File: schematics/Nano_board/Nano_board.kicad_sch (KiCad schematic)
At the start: 28 parts, among them J1 Screw_Terminal_01x02, J2 Screw_Terminal_01x02, J3 Screw_Terminal_01x02, J4 Left switch, J5 Right switch, J6 UART, J7 Left encoder, J8 Right encoder

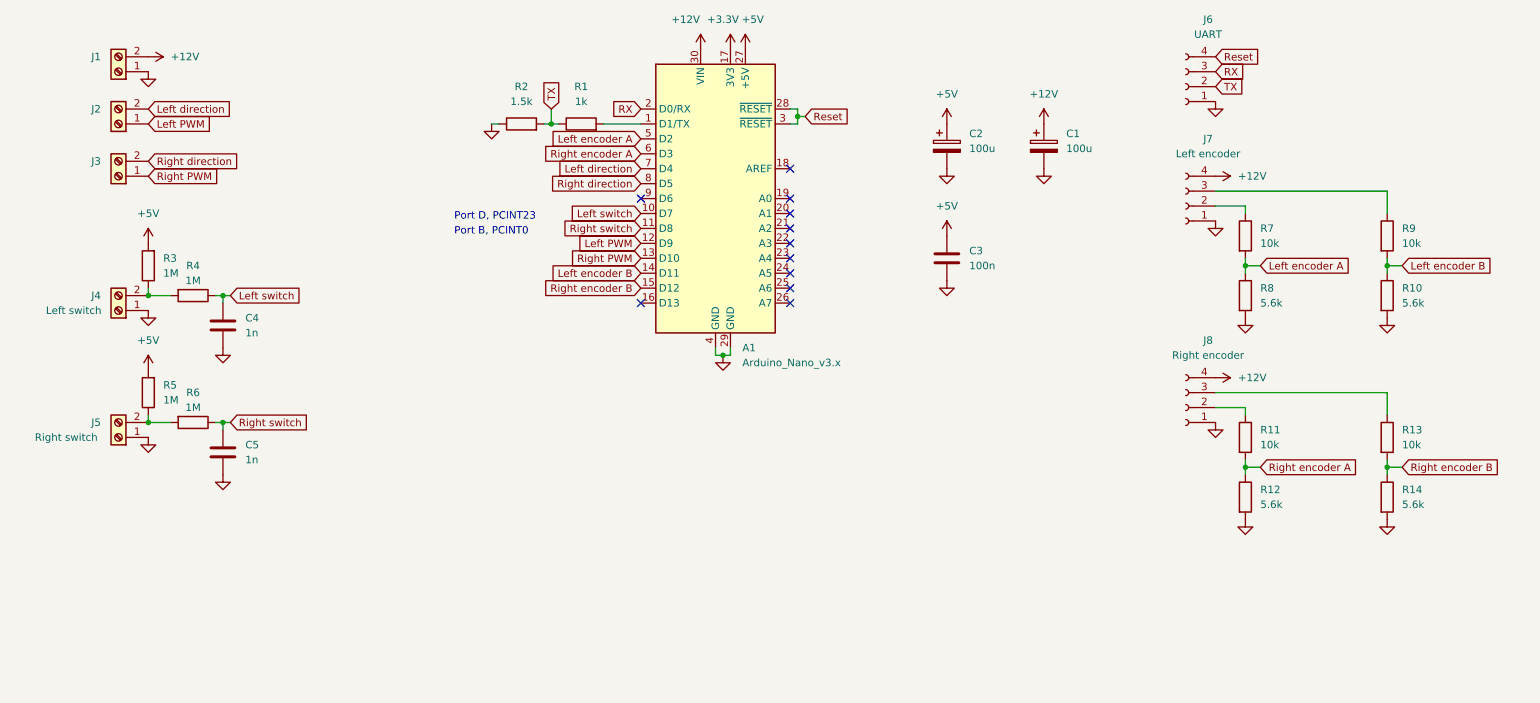
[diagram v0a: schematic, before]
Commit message: feat: updated Nano board schematics.
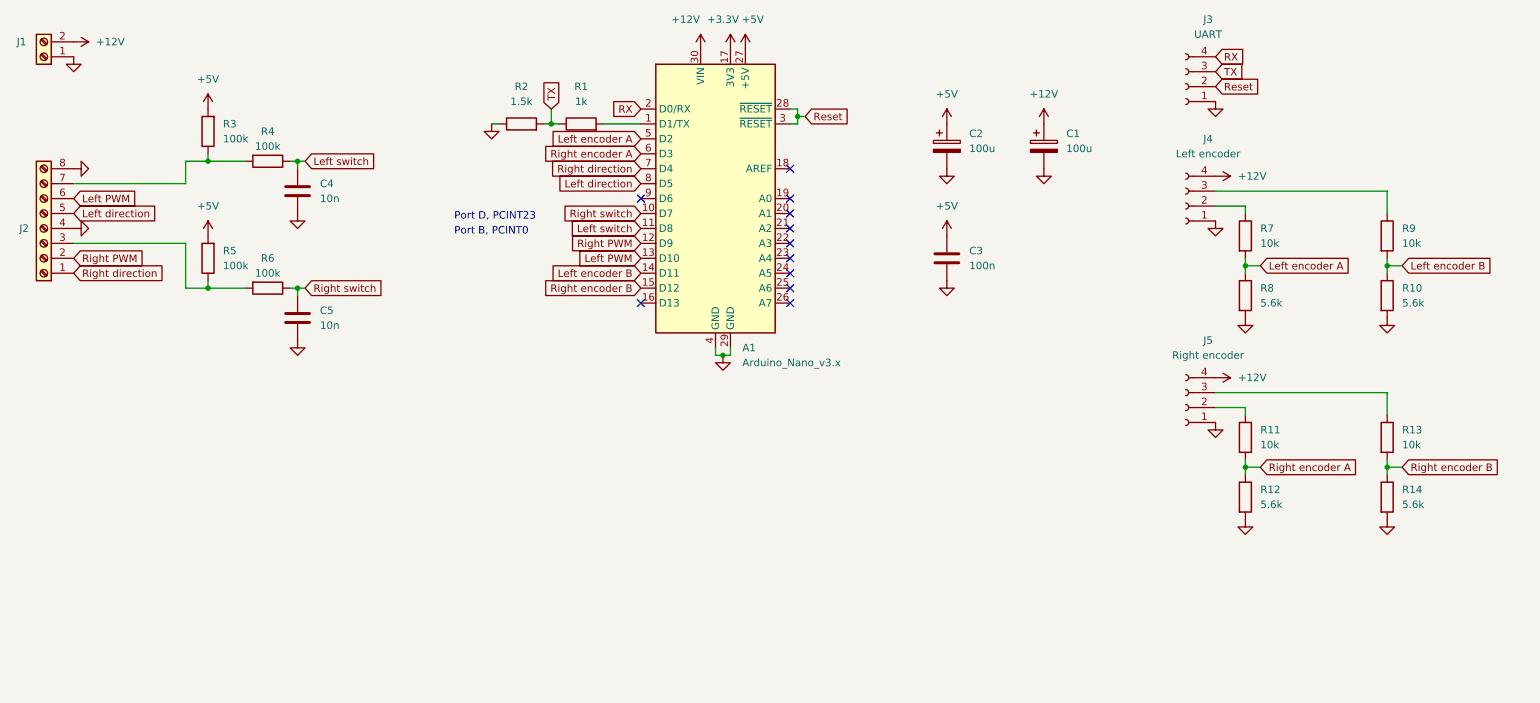
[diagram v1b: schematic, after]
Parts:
- removed J2, J3: Screw_Terminal_01x02, symbol Connector:Screw_Terminal_01x02
- removed J4: Left switch, symbol Connector:Screw_Terminal_01x02
- removed J5: Right switch, symbol Connector:Screw_Terminal_01x02
- added J2: Screw_Terminal_01x08, symbol Connector:Screw_Terminal_01x08
- C4, C5: value 1n -> 10n
- R3, R4, R5, R6: value 1M -> 100k
- renumbered J6 to J3, J7 to J4, J8 to J5
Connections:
- net GND: now also J2.4 (Pin_4), J2.8 (Pin_8)
- net Left PWM: now also A1.13 (D10), J2.6 (Pin_6); no longer A1.12 (D9)
- net Left direction: now also A1.8 (D5), J2.5 (Pin_5); no longer A1.7 (D4)
- net Left switch: now also A1.11 (D8); no longer A1.10 (D7)
- net RX: now also J3.4 (Pin_4); no longer J3.3 (Pin_3)
- net Reset: now also J3.2 (Pin_2); no longer J3.4 (Pin_4)
- net Right PWM: now also A1.12 (D9), J2.2 (Pin_2); no longer A1.13 (D10)
- net Right direction: now also A1.7 (D4), J2.1 (Pin_1); no longer A1.8 (D5)
- net Right switch: now also A1.10 (D7); no longer A1.11 (D8)
- net TX: now also J3.3 (Pin_3); no longer J3.2 (Pin_2)
- net at R3.1, R4.2: now also J2.7 (Pin_7)
- net at R5.1, R6.2: now also J2.3 (Pin_3)
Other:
- moved on the sheet: C4, C5, J1, R3, R4, R5, R6

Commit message: feat: fixed schematics and updated LMD18200 library.
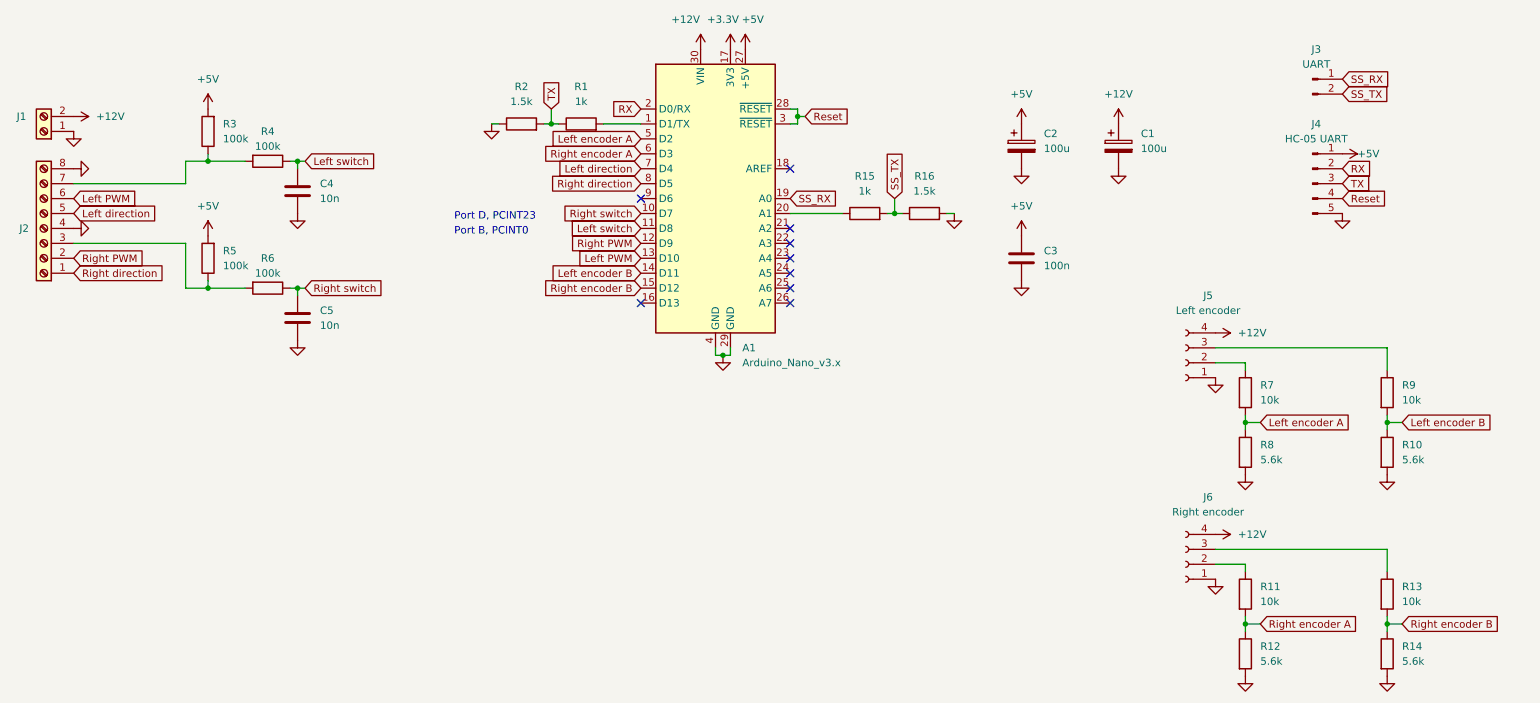
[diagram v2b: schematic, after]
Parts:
- removed J3: UART, symbol Connector:Conn_01x04_Female
- removed J5: Right encoder, symbol Connector:Conn_01x04_Female
- added J3: UART, symbol Connector:Conn_01x02_Male
- added J4: HC-05 UART, symbol Connector:Conn_01x05_Male
- added J6: Right encoder, symbol Connector:Conn_01x04_Female
- added R15: 1k, symbol Device:R
- added R16: 1.5k, symbol Device:R
- renumbered J4 to J5
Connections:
- net +12V: now also J6.4 (Pin_4)
- net +5V: now also J4.1 (Pin_1)
- net GND: now also J4.5 (Pin_5), J6.1 (Pin_1), R16.2
- net Left direction: now also A1.7 (D4); no longer A1.8 (D5)
- net RX: now also J4.2 (Pin_2)
- net Reset: now also J4.4 (Pin_4)
- net Right direction: now also A1.8 (D5); no longer A1.7 (D4)
- net TX: now also J4.3 (Pin_3)
- net SS_RX: now reaches A1.19 (A0)
- net SS_RX: now also J3.1 (Pin_1)
- net at A1.20 (A1): now also R15.1
- net at R13.1: now also J6.3 (Pin_3)
- net at R11.1: now also J6.2 (Pin_2)
- new net SS_TX: J3.2 (Pin_2), R15.2, R16.1
- no-connect marks 11 -> 9
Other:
- moved on the sheet: C1, C2, C3, J1, J5, R10, R11, R12, R13, R14, R7, R8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
